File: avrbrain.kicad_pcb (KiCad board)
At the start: 4 copper layers, 85 x 56 mm, 45 parts, among them J1 XKTF-0803-0, J12 PD/PE, J2 U254-051T-4BH81-S2S, J3 SM04B-SRSS-TB, J4 UPDI, J5 UEXT, J6 PIHAT, J7 PG/PB, J9 SM04B-SRSS-TB, Q1 BSS138, Q2 BSS138, SW1 RESET, U1 CH340C, U2 AVR128DB64x-xPT, U3 PCF8563T, U5 AMS1117-3.3, Y1 32kHz, Y2 32kHz

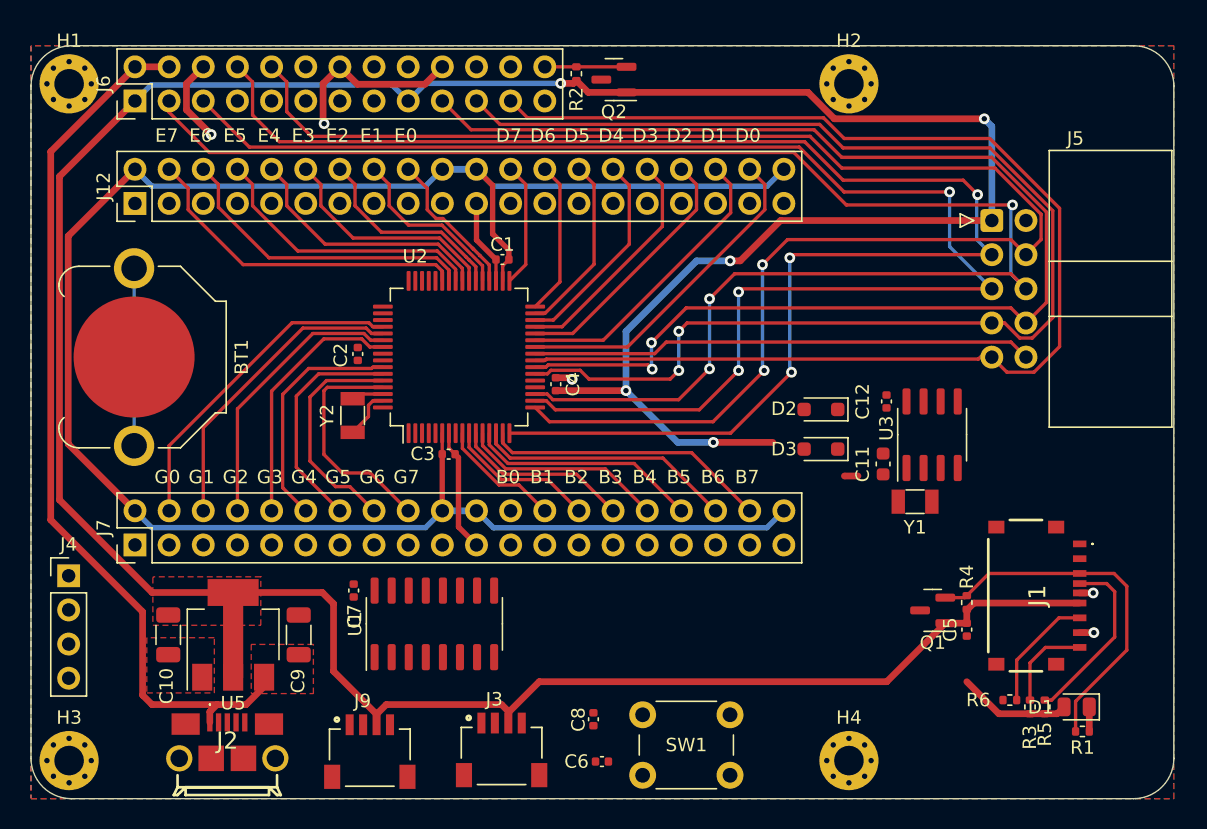
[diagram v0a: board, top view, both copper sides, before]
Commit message: Tweaks to layout, finish all connections
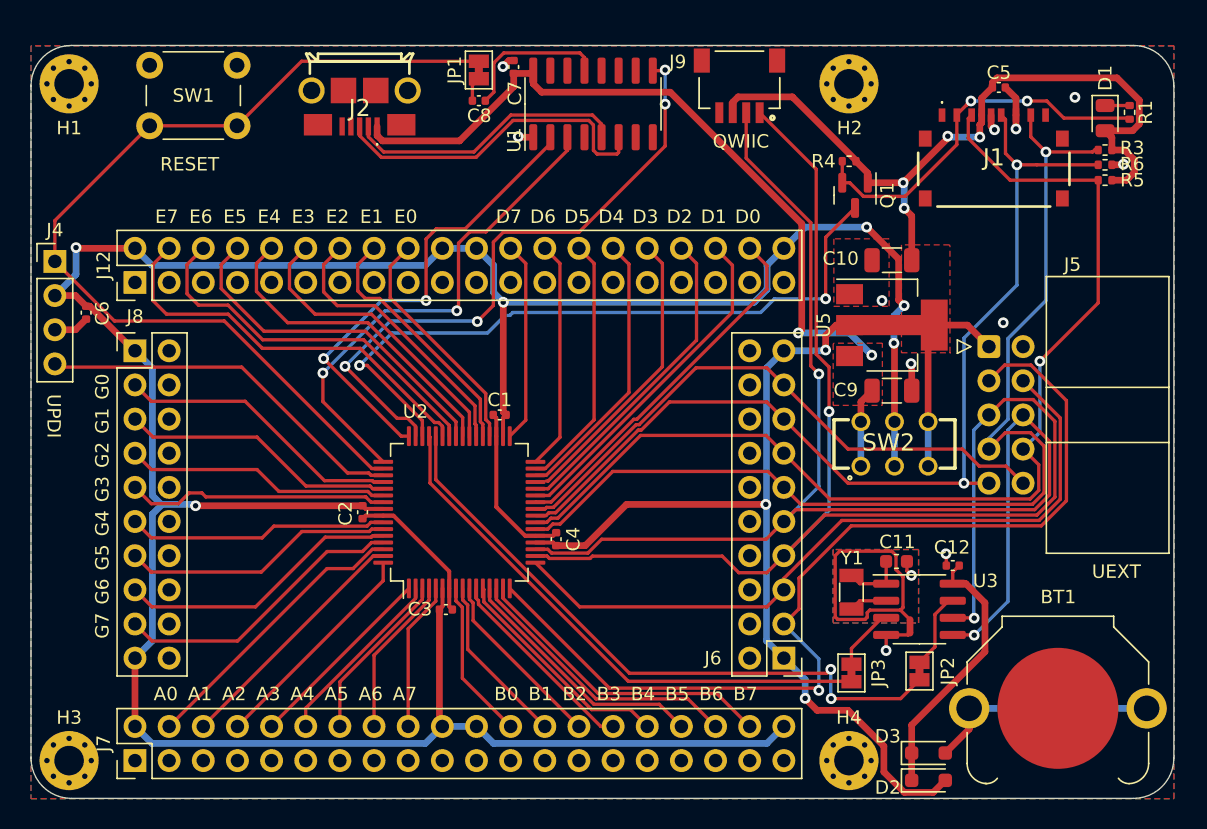
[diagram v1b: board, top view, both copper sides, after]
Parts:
- removed J3: SM04B-SRSS-TB, Custom:JST_SM04B-SRSS-TB_LF__SN_
- removed Q2: BSS138, Package_TO_SOT_SMD:SOT-23
- removed R2: 100K, Resistor_SMD:R_0402_1005Metric
- removed Y2: 32kHz, Crystal:Crystal_SMD_3215-2Pin_3.2x1.5mm
- added J8: PG, Connector_PinHeader_2.54mm:PinHeader_2x10_P2.54mm_Vertical, F.Cu at (129.7, 103.7)
- added JP1: AUTORESET, Jumper:SolderJumper-2_P1.3mm_Bridged_Pad1.0x1.5mm, F.Cu at (155.3, 82.8)
- added JP2: CLK32K, Jumper:SolderJumper-2_P1.3mm_Bridged_Pad1.0x1.5mm, F.Cu at (188.1, 127.5)
- added JP3: RTCINT, Jumper:SolderJumper-2_P1.3mm_Bridged_Pad1.0x1.5mm, F.Cu at (183.0, 127.7)
- added SW2: VDD, SamacSys_Parts:JS202011CQN, F.Cu at (186.2, 110.6)
- J6: value PIHAT -> PC; footprint Connector_PinHeader_2.54mm:PinHeader_2x13_P2.54mm_Vertical -> Connector_PinHeader_2.54mm:PinHeader_2x10_P2.54mm_Vertical
- J7: value PG/PB -> PA/PB
- moved BT1 73.5 mm to (198.4, 130.3), turned to 0 degrees
- moved J6 63.6 mm to (178.0, 126.5), turned to 180 degrees
- moved SW1 60.6 mm to (130.8, 82.5)
- moved C10 60.6 mm to (186.0, 97.0), turned to 180 degrees
- moved U5 54.1 mm to (186.0, 101.8), turned to 0 degrees
- moved J9 53.2 mm to (174.7, 86.0), turned to 180 degrees
- moved C6 50.9 mm to (126.1, 100.9), turned to -90 degrees
- moved J2 50.0 mm to (146.4, 84.6), turned to 180 degrees
- moved C9 47.7 mm to (186.0, 106.7), turned to 0 degrees
- moved C8 46.8 mm to (155.3, 85.1), turned to 180 degrees
- moved R1 46.2 mm to (203.7, 86.0), turned to 90 degrees
- moved D1 43.8 mm to (201.9, 86.4), turned to -90 degrees
- moved R3 41.8 mm to (201.9, 88.8), turned to 180 degrees
- moved C7 40.7 mm to (157.9, 82.6)
- moved R6 40.4 mm to (201.9, 89.9), turned to 180 degrees
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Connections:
- C6 pad 1: Net-(J4-Pin_2) -> VDD
- C6 pad 2: Net-(J4-Pin_3) -> GND
- C8 pad 1: unconnected-(C8-Pad1) -> /~{DTR}
- C8 pad 2: unconnected-(C8-Pad2) -> Net-(JP1-A)
- D2 pad 2: VDD -> +3.3V
- J1 pad P2: unconnected-(J1-DAT3/CD-PadP2) -> Net-(J1-DAT3/CD)
- J1 pad P3: Net-(J1-CMD) -> /MOSI
- J1 pad P4: /MOSI -> +3.3V
- J1 pad P5: +3.3V -> /SCK
- J1 pad P6: /SCK -> GND
- J1 pad P7: GND -> /MISO
- J1 pad P8: /MISO -> unconnected-(J1-DAT1-PadP8)
- J4 pad 2: Net-(J4-Pin_2) -> VDD
- J4 pad 3: Net-(J4-Pin_3) -> GND
- J5 pad 5: /SCL3V -> /SCL
- J5 pad 6: /SDA3V -> /SDA
- J6 pad 10: /RX3V -> GND
- J6 pad 11: unconnected-(J6-Pin_11-Pad11) -> /MISO
- J6 pad 12: unconnected-(J6-Pin_12-Pad12) -> GND
- J6 pad 13: unconnected-(J6-Pin_13-Pad13) -> /MOSI
- J6 pad 15: unconnected-(J6-Pin_15-Pad15) -> /SCK
- J6 pad 16: unconnected-(J6-Pin_16-Pad16) -> GND
- J6 pad 17: +3.3V -> /~{UXCS}
- J6 pad 18: unconnected-(J6-Pin_18-Pad18) -> GND
- J6 pad 19: /MOSI -> +3.3V
- J6 pad 2: +5V -> GND
- J6 pad 3: /SDA3V -> /TX3V
- J6 pad 4: +5V -> GND
- J6 pad 5: /SCL3V -> /RX3V
- J6 pad 7: unconnected-(J6-Pin_7-Pad7) -> /SCL
- J6 pad 8: /TX3V -> GND
- J6 pad 9: GND -> /SDA
- J7 pad 10: /PG3 -> /PA3
- J7 pad 12: /PG4 -> /PA4
- J7 pad 14: /PG5 -> /PA5
- J7 pad 16: /PG6 -> /PA6
- J7 pad 18: /PG7 -> /PA7
- J7 pad 4: /PG0 -> /PA0
- J7 pad 6: /PG1 -> /PA1
- J7 pad 8: /PG2 -> /PA2
- J9 pad 1: /SCL3V -> /SCL
- J9 pad 2: /SDA3V -> /SDA
- Q1 pad 2: Net-(J1-CMD) -> Net-(J1-DAT3/CD)
- R1 pad 1: Net-(J1-CMD) -> Net-(J1-DAT3/CD)
- R4 pad 2: Net-(J1-CMD) -> Net-(J1-DAT3/CD)
- U1 pad 10: /~{DSR} -> unconnected-(U1-~{DSR}-Pad10)
- U1 pad 11: /~{RI} -> unconnected-(U1-~{RI}-Pad11)
- U1 pad 12: /~{DCD} -> unconnected-(U1-~{DCD}-Pad12)
- U1 pad 2: /RX5V -> /RXU
- U1 pad 3: /TX5V -> /TXU
- U2 pad 1: /~{CTS} -> /PA3
- U2 pad 18: /SCL3V -> /SCL
- U2 pad 19: /SDA3V -> /SDA
- U2 pad 2: /RX5V -> /PA4
- U2 pad 3: /TX5V -> /PA5
- U2 pad 4: unconnected-(U2-PA6-Pad4) -> /PA6
- U2 pad 45: unconnected-(U2-XTAL32K2/PF1-Pad45) -> /~{RTCINT}
- U2 pad 46: /SCL5V -> /~{SDCS}
- U2 pad 47: /SDA5V -> /~{CTS}
- U2 pad 48: /~{PHCS} -> /RXU
- U2 pad 49: /~{SDCS} -> /TXU
- U2 pad 5: unconnected-(U2-PA7-Pad5) -> /PA7
- U2 pad 62: Net-(U2-XTALHF1/PA0) -> /PA0
- U2 pad 63: Net-(U2-XTALHF2/PA1) -> /PA1
- U2 pad 64: /~{RTS} -> /PA2
- U3 pad 3: /~{RTCINT} -> Net-(JP3-B)
- U3 pad 5: /SDA5V -> /SDA
- U3 pad 6: /SCL5V -> /SCL
- U3 pad 7: /CLK32K -> Net-(JP2-B)
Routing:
- net +3.3V: track 265.6 -> 146.1 mm, vias 5 -> 7
- net /SDA3V: track 117.3 -> 0.00 mm, vias 3 -> 0
- net /SCL3V: track 108.2 -> 0.00 mm, vias 3 -> 0
- net /SCL: track 0.00 -> 107.0 mm, vias 0 -> 2
- net /SDA: track 0.00 -> 100.1 mm, vias 0 -> 2
- net Net-(J4-Pin_1): track 0.00 -> 70.3 mm
- net VDD: track 145.5 -> 214.3 mm, vias 0 -> 6
- net /RX3V: track 114.3 -> 54.2 mm, vias 2 -> 0
- net /~{SDCS}: track 0.00 -> 51.9 mm, vias 0 -> 2
- net /CLK32K: track 0.00 -> 48.0 mm, vias 0 -> 2
- net /~{CTS}: track 0.00 -> 47.8 mm, vias 0 -> 4
- net /~{RTCINT}: track 0.00 -> 41.1 mm
- net /TX3V: track 111.9 -> 73.1 mm, vias 3 -> 1
- net /TXU: track 0.00 -> 37.4 mm, vias 0 -> 2
- net /RXU: track 0.00 -> 35.4 mm, vias 0 -> 2
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- added copper zone on B.Cu, net GND1
- added copper zone on F.Cu, net GND1
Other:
- copper layers 4 -> 2
- board text added: "A0"
- board text added: "A1"
- board text added: "A2"
- board text added: "A3"
- board text added: "A4"
- board text added: "A5"
- board text added: "A6"
- board text added: "A7"
- board text added: "AVRbrain Copyright (C)2024 J.B. Langston III https://github.com/jblang/avrbrain"
- board text added: "QWIIC"
- board text added: "RESET"
- board text added: "UEXT"
- board text added: "UPDI"

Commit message: Finish layout and routing
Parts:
- removed SW2: VDD, SamacSys_Parts:JS202011CQN
- removed U5: AMS1117-3.3, Package_TO_SOT_SMD:SOT-223-3_TabPin2
- added C13: 27pf, Capacitor_SMD:C_0603_1608Metric_Pad1.08x0.95mm_HandSolder, F.Cu at (200.9, 124.6)
- added C14: 0.1uf, Capacitor_SMD:C_0402_1005Metric, F.Cu at (205.1, 124.8)
- added C15: 22uf, Capacitor_SMD:C_1206_3216Metric, F.Cu at (177.2, 85.0)
- added D4: 1N5819WS, Diode_SMD:D_SOD-323_HandSoldering, F.Cu at (193.8, 124.0)
- added J11: UEXT, Connector_IDC:IDC-Header_2x05_P2.54mm_Horizontal, F.Cu at (184.9, 94.9)
- added J3: PORTG, Connector_PinSocket_2.54mm:PinSocket_2x09_P2.54mm_Vertical, F.Cu at (132.1, 106.7)
- added JP4: VDD_MAIN, Jumper:SolderJumper-3_P1.3mm_Bridged2Bar12_RoundedPad1.0x1.5mm, F.Cu at (163.7, 93.5)
- added JP5: VDD_MVIO, Jumper:SolderJumper-3_P1.3mm_Bridged2Bar12_RoundedPad1.0x1.5mm, F.Cu at (175.9, 93.5)
- added JP6: RTC_CLK, Jumper:SolderJumper-2_P1.3mm_Bridged_RoundedPad1.0x1.5mm, F.Cu at (191.1, 119.2)
- added JP7: RTC_INT, Jumper:SolderJumper-2_P1.3mm_Bridged_RoundedPad1.0x1.5mm, F.Cu at (193.7, 119.2)
- added R10: 2.2K, Resistor_SMD:R_0402_1005Metric, F.Cu at (193.7, 115.1)
- added R2: 1K, Resistor_SMD:R_0402_1005Metric, F.Cu at (201.6, 102.7)
- added R7: 2.2K, Resistor_SMD:R_0402_1005Metric, F.Cu at (188.5, 115.1)
- added R8: 2.2K, Resistor_SMD:R_0402_1005Metric, F.Cu at (186.0, 115.1)
- added R9: 2.2K, Resistor_SMD:R_0402_1005Metric, F.Cu at (191.1, 115.1)
- added SW3: PROG_EN, SamacSys_Parts:JS202011CQN, F.Cu at (153.7, 86.4)
- added U4: PCF8563T, Package_SO:SOIC-8_3.9x4.9mm_P1.27mm, F.Cu at (202.6, 128.1)
- C10, C9: value 1uf -> 0.1uf; footprint Capacitor_SMD:C_1206_3216Metric -> Capacitor_SMD:C_0402_1005Metric
- C11: value 27pf -> 0.1uf; footprint Capacitor_SMD:C_0603_1608Metric -> Capacitor_SMD:C_0402_1005Metric
- C12, C7: value 0.1uf -> 1uf; footprint Capacitor_SMD:C_0402_1005Metric -> Capacitor_SMD:C_1206_3216Metric
- C6: value 0.1uf -> 22uf; footprint Capacitor_SMD:C_0402_1005Metric -> Capacitor_SMD:C_1206_3216Metric
- D1: value LED -> 1N5819WS; footprint LED_SMD:LED_0805_2012Metric -> Diode_SMD:D_SOD-323_HandSoldering
- D2: value 1N5819WS -> LED; footprint Diode_SMD:D_SOD-323_HandSoldering -> LED_SMD:LED_0805_2012Metric
- J1: value XKTF-0803-0 -> UPDI; footprint SamacSys_Parts:XKTF08030 -> Connector_PinHeader_2.54mm:PinHeader_1x04_P2.54mm_Vertical
- J12: value PD/PE -> SM04B-SRSS-TB; footprint Connector_PinHeader_2.54mm:PinHeader_2x20_P2.54mm_Vertical -> Custom:JST_SM04B-SRSS-TB_LF__SN_
- J2: value U254-051T-4BH81-S2S -> PORTD; footprint SamacSys_Parts:U254051T4BH81S2S -> Connector_PinSocket_2.54mm:PinSocket_2x09_P2.54mm_Vertical
- J4: value UPDI -> PORTE; footprint Connector_PinHeader_2.54mm:PinHeader_1x04_P2.54mm_Vertical -> Connector_PinSocket_2.54mm:PinSocket_2x09_P2.54mm_Vertical
- J5: value UEXT -> PORTA; footprint Connector_IDC:IDC-Header_2x05_P2.54mm_Horizontal -> Connector_PinSocket_2.54mm:PinSocket_2x09_P2.54mm_Vertical
- J6: value PC -> PORTB; footprint Connector_PinHeader_2.54mm:PinHeader_2x10_P2.54mm_Vertical -> Connector_PinSocket_2.54mm:PinSocket_2x09_P2.54mm_Vertical
- J7: value PA/PB -> PORTC; footprint Connector_PinHeader_2.54mm:PinHeader_2x20_P2.54mm_Vertical -> Connector_PinSocket_2.54mm:PinSocket_2x09_P2.54mm_Vertical
- J8: value PG -> XKTF-0803-0; footprint Connector_PinHeader_2.54mm:PinHeader_2x10_P2.54mm_Vertical -> SamacSys_Parts:XKTF08030
- J9: value SM04B-SRSS-TB -> U254-051T-4BH81-S2S; footprint Custom:JST_SM04B-SRSS-TB_LF__SN_ -> SamacSys_Parts:U254051T4BH81S2S
- JP1: footprint Jumper:SolderJumper-2_P1.3mm_Bridged_Pad1.0x1.5mm -> Jumper:SolderJumper-2_P1.3mm_Bridged_RoundedPad1.0x1.5mm
- JP2: value CLK32K -> RTC_SCL; footprint Jumper:SolderJumper-2_P1.3mm_Bridged_Pad1.0x1.5mm -> Jumper:SolderJumper-2_P1.3mm_Bridged_RoundedPad1.0x1.5mm
- JP3: value RTCINT -> RTC_SDA; footprint Jumper:SolderJumper-2_P1.3mm_Bridged_Pad1.0x1.5mm -> Jumper:SolderJumper-2_P1.3mm_Bridged_RoundedPad1.0x1.5mm
- R1: value 1K -> 4.7K
- U1: value CH340C -> AVR128DB64x-xPT; footprint Package_SO:SOIC-16_3.9x9.9mm_P1.27mm -> Package_QFP:TQFP-64_10x10mm_P0.5mm
- U2: value AVR128DB64x-xPT -> AMS1117-3.3; footprint Package_QFP:TQFP-64_10x10mm_P0.5mm -> Package_TO_SOT_SMD:SOT-223-3_TabPin2
- U3: value PCF8563T -> CH340C; footprint Package_SO:SOIC-8_3.9x4.9mm_P1.27mm -> Package_SO:SOIC-16_3.9x9.9mm_P1.27mm
- moved J12 72.4 mm to (202.0, 93.6)
- moved J8 70.2 mm to (199.5, 111.2), turned to 90 degrees
- moved J5 69.9 mm to (129.6, 132.1), turned to 90 degrees
- moved J1 69.8 mm to (124.5, 99.1), turned to 0 degrees
- moved C11 57.4 mm to (137.7, 88.9)
- moved U3 56.5 mm to (142.5, 89.5)
- moved D1 49.5 mm to (152.5, 90.0), turned to 180 degrees
- moved C5 48.8 mm to (159.8, 118.8), turned to 90 degrees
- moved R1 48.2 mm to (155.7, 90.0), turned to 180 degrees
- moved J7 43.6 mm to (172.7, 127.0), turned to 180 degrees
- moved C10 43.2 mm to (145.0, 83.6)
- moved J9 41.6 mm to (133.1, 84.1)
- moved C6 39.7 mm to (162.4, 85.0)
- moved C12 38.1 mm to (174.8, 85.0), turned to 90 degrees
- moved D2 37.3 mm to (205.3, 102.2)
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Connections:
- C10 pad 1: +3.3V -> +5V
- C11 pad 1: GND1 -> Net-(U3-V3)
- C11 pad 2: Net-(U3-OSCI) -> GND
- C12 pad 1: Net-(D2-K) -> +3.3V
- C4 pad 1: +3.3V -> VDD
- C5 pad 1: +3.3V -> VDDF
- C6 pad 1: VDD -> +5V
- C8 pad 1: /~{DTR} -> Net-(U3-~{DTR})
- C9 pad 1: +5V -> +3.3V
- D1 pad 2: +3.3V -> UPDI
- D3 pad 1: Net-(D2-K) -> Net-(D3-K)
- D3 pad 2: Net-(BT1-+) -> +3.3V
- J12 pad 1: GND -> SCL
- J12 pad 2: VDD -> SDA
- J12 pad 3: GND -> +3.3V
- J12 pad 4: /PE7 -> GND
- J2 pad 1: +5V -> VDD
- J2 pad 2: Net-(J2-D-) -> GND
- J2 pad 3: Net-(J2-D+) -> /PD0
- J2 pad 4: unconnected-(J2-ID-Pad4) -> GND
- J2 pad 5: GND -> /PD1
- J4 pad 1: Net-(J4-Pin_1) -> VDD
- J4 pad 2: VDD -> GND
- J4 pad 3: GND -> /PE0
- J4 pad 4: Net-(J4-Pin_4) -> GND
- J5 pad 1: +3.3V -> VDD
- J5 pad 10: /~{UXCS} -> GND
- J5 pad 3: /TX3V -> /PA0
- J5 pad 4: /RX3V -> GND
- J5 pad 5: /SCL -> /PA1
- J5 pad 6: /SDA -> GND
- J5 pad 7: /MISO -> /PA2
- J5 pad 8: /MOSI -> GND
- J5 pad 9: /SCK -> /PA3
- J6 pad 1: +3.3V -> VDD
- J6 pad 11: /MISO -> /PB4
- J6 pad 13: /MOSI -> /PB5
- J6 pad 15: /SCK -> /PB6
- J6 pad 17: /~{UXCS} -> /PB7
- J6 pad 3: /TX3V -> /PB0
- J6 pad 5: /RX3V -> /PB1
- J6 pad 7: /SCL -> /PB2
- J6 pad 9: /SDA -> /PB3
- J7 pad 1: GND -> VDDF
- J7 pad 10: /PA3 -> GND
- J7 pad 11: GND -> MISO
- J7 pad 12: /PA4 -> GND
- J7 pad 13: GND -> MOSI
- J7 pad 14: /PA5 -> GND
- J7 pad 15: GND -> SCK
- J7 pad 16: /PA6 -> GND
- J7 pad 17: GND -> ~{CS}
- J7 pad 18: /PA7 -> GND
- J7 pad 2: VDD -> GND
- J7 pad 3: GND -> TXC
- J7 pad 4: /PA0 -> GND
- J7 pad 5: GND -> RXC
- J7 pad 6: /PA1 -> GND
- J7 pad 7: GND -> SDA
- J7 pad 8: /PA2 -> GND
- J7 pad 9: GND -> SCL
- J9 pad 1: /SCL -> unconnected-(J9-VBUS-Pad1)
- J9 pad 2: /SDA -> /Peripherals/UD-
- J9 pad 3: +3.3V -> /Peripherals/UD+
- J9 pad 4: GND -> unconnected-(J9-ID-Pad4)
- JP1 pad 2: Net-(J4-Pin_1) -> ~{RESET}
- JP2 pad 1: /CLK32K -> SCL
- JP3 pad 1: /~{RTCINT} -> SDA
- Q1 pad 2: Net-(J1-DAT3/CD) -> ~{SDCS}
- Q1 pad 3: /~{SDCS} -> Net-(J8-DAT3/CD)
- R1 pad 1: Net-(J1-DAT3/CD) -> Net-(SW3A-C)
- R3 pad 2: /MISO -> Net-(J8-DAT3/CD)
- R4 pad 2: Net-(J1-DAT3/CD) -> MOSI
- R5 pad 1: +3.3V -> GND
- R5 pad 2: /MOSI -> SCK
- R6 pad 1: GND -> +3.3V
- R6 pad 2: /SCK -> MISO
- SW1 pad 2: Net-(J4-Pin_1) -> ~{RESET}
- U1 pad 1: GND -> /PA3
- U1 pad 10: unconnected-(U1-~{DSR}-Pad10) -> /PB2
- U1 pad 11: unconnected-(U1-~{RI}-Pad11) -> /PB3
- U1 pad 12: unconnected-(U1-~{DCD}-Pad12) -> /PB4
- U1 pad 13: /~{DTR} -> /PB5
- U1 pad 14: /~{RTS} -> /PB6
- U1 pad 15: unconnected-(U1-R232-Pad15) -> /PB7
- U1 pad 16: +5V -> TXC
- U1 pad 2: /RXU -> /PA4
- U1 pad 3: /TXU -> /PA5
- U1 pad 4: unconnected-(U1-V3-Pad4) -> /PA6
- U1 pad 5: Net-(J2-D-) -> /PA7
- U1 pad 6: Net-(J2-D+) -> VDD
- U1 pad 7: unconnected-(U1-NC-Pad7) -> GND
- U1 pad 8: unconnected-(U1-NC-Pad8) -> /PB0
- U1 pad 9: /~{CTS} -> /PB1
- U2 pad 1: /PA3 -> GND
- U2 pad 2: /PA4 -> +3.3V
- U2 pad 3: /PA5 -> +5V
- U3 pad 1: Net-(U3-OSCI) -> GND
- U3 pad 2: Net-(U3-OSCO) -> /Peripherals/USBTX
- U3 pad 3: Net-(JP3-B) -> /Peripherals/USBRX
- U3 pad 4: GND -> Net-(U3-V3)
- U3 pad 5: /SDA -> /Peripherals/UD-
- U3 pad 6: /SCL -> /Peripherals/UD+
- U3 pad 7: Net-(JP2-B) -> unconnected-(U3-NC-Pad7)
- U3 pad 8: Net-(D2-K) -> unconnected-(U3-NC-Pad8)
- Y1 pad 1: Net-(U3-OSCO) -> Net-(U4-OSCO)
- Y1 pad 2: Net-(U3-OSCI) -> Net-(U4-OSCI)
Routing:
- net /SCL: track 107.0 -> 0.00 mm, vias 2 -> 0
- net /SDA: track 100.1 -> 0.00 mm, vias 2 -> 0
- net SDA: track 0.00 -> 93.4 mm, vias 0 -> 2
- net SCL: track 0.00 -> 87.6 mm, vias 0 -> 2
- net SCK: track 0.00 -> 86.8 mm, vias 0 -> 2
- net /MOSI: track 81.0 -> 0.00 mm, vias 1 -> 0
- net /MISO: track 80.5 -> 0.00 mm, vias 1 -> 0
- net MOSI: track 0.00 -> 80.4 mm, vias 0 -> 4
- net TXC: track 0.00 -> 77.3 mm, vias 0 -> 1
- net MISO: track 0.00 -> 76.0 mm, vias 0 -> 2
- net /SCK: track 75.3 -> 0.00 mm, vias 2 -> 0
- net /TX3V: track 73.1 -> 0.00 mm, vias 1 -> 0
- net Net-(J4-Pin_1): track 70.3 -> 0.00 mm
- net RXC: track 0.00 -> 68.5 mm, vias 0 -> 1
- net ~{SDCS}: track 0.00 -> 67.2 mm, vias 0 -> 4
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- removed copper zone on F.Cu, net GND1
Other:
- board text added: "1117-3.3"
- board text added: "3.3V"
- board text added: "5V"
- board text added: "C0"
- board text added: "C1"
- board text added: "C2"
- board text added: "C3"
- board text added: "C4"
- board text added: "C5"
- board text added: "C6"
- board text added: "C7"
- board text added: "CH340C"
- board text added: "CLK"
- board text added: "COMM"
- board text added: "CR1216"
- board text added: "Copyright (C)2024 J.B. Langston III https://github.com/jblang/avrbrain"
- board text added: "I2C"
- board text added: "MAIN"
- board text added: "MICRO SD"
- board text added: "MVDD"
- board text added: "MVIO"
- board text added: "PCF8563"
- board text added: "PROG"
- board text added: "SCL"
- board text added: "SDA"
- board text added: "UEXT 3.3V ONLY"
- board text added: "USB"
- board text added: "VDD"
- board text added: "~{DTR}"
- board text added: "~{INT}"
- board text added: "~{RESET}"
- board text removed: "AVRbrain Copyright (C)2024 J.B. Langston III https://github.com/jblang/avrbrain"
- board text removed: "QWIIC"
- board text removed: "UEXT"
